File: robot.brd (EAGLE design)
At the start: 63.2 x 48.2 mm, 17 parts

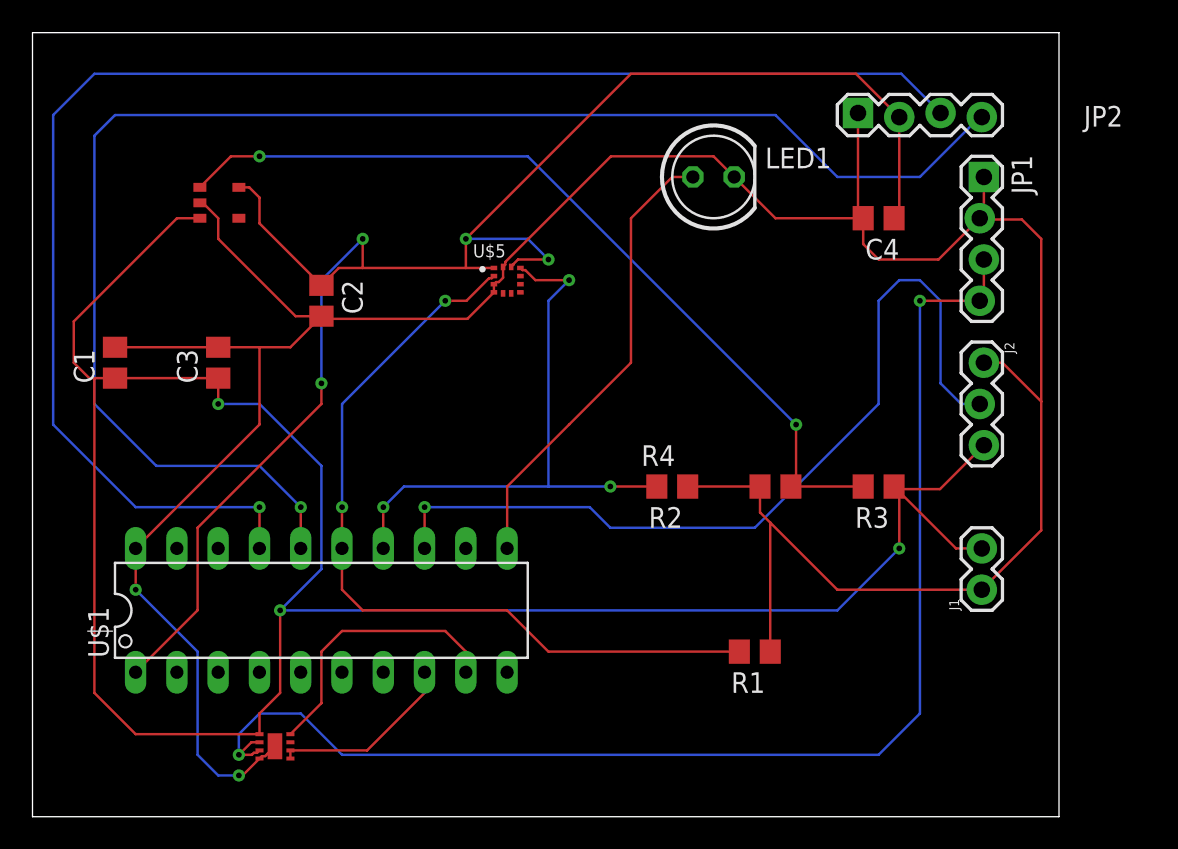
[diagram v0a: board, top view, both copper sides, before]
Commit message: Added power planes to board and also added a resistor for the LED.
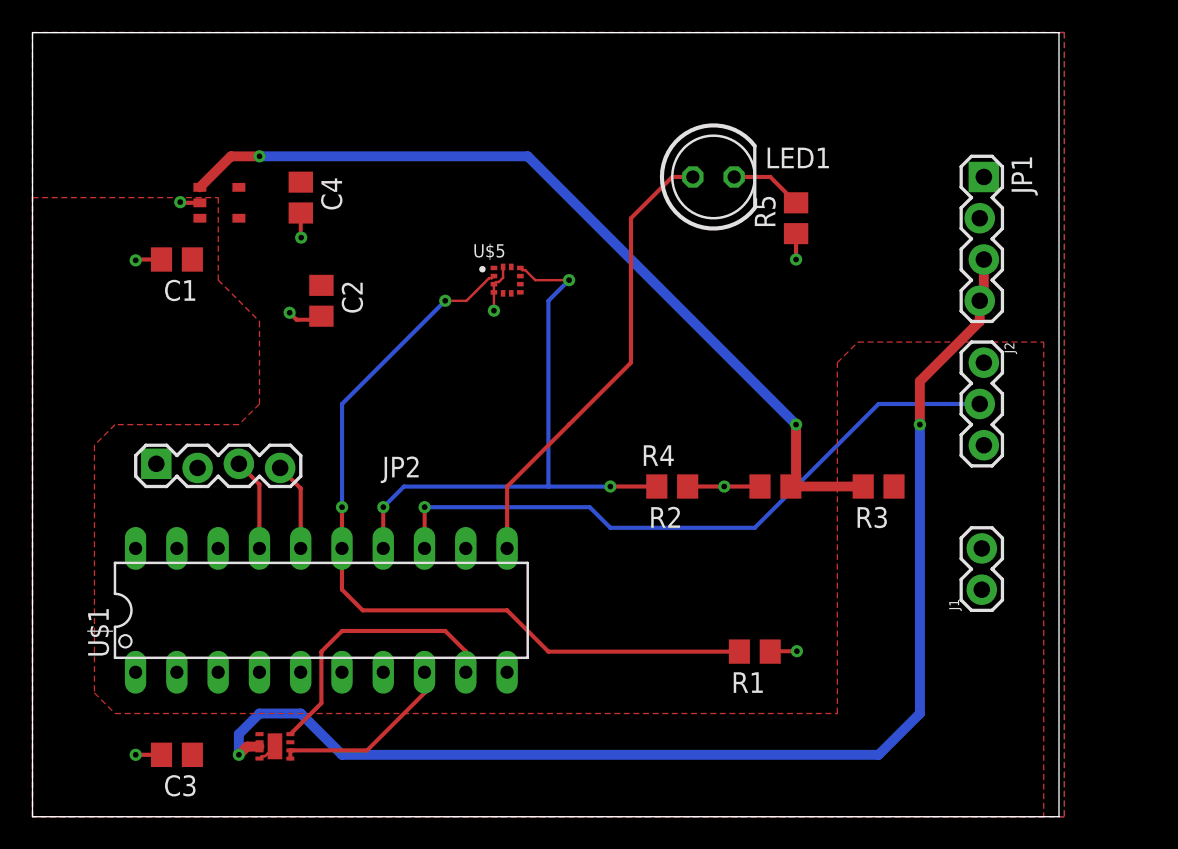
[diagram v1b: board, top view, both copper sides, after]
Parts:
- added R5: 330, rcl:R0805
- moved JP2 48.3 mm to (7.62, 48.3)
- moved C4 35.6 mm to (16.5, 64.8), turned to 270 degrees
- moved C3 24.3 mm to (8.89, 30.5), turned to 180 degrees
- moved C1 7.41 mm to (8.89, 61.0), turned to 180 degrees
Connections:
- net N$5 renamed 3V3_RAW
- net N$8 renamed MOTOR
- new net N$3: LED1.K, R5.2
- net 0: now also R5.1; no longer LED1.K
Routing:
- net 0: track 181.5 -> 20.7 mm, vias 2 -> 9
- net 4V5: track 137.5 -> 0.68 mm, vias 3 -> 0
- net 3V3: track 102.1 -> 0.00 mm, vias 4 -> 0
- net N$10: track 93.1 -> 5.73 mm, vias 1 -> 0
- net N$11: track 92.6 -> 5.48 mm, vias 1 -> 0
- net PWM_TA1.2: track 53.4 -> 40.4 mm
- net N$3: track 0.00 -> 4.47 mm
- net MOTOR: track 80.5 -> 77.4 mm
- added copper zone on layer 16, net 0
- added copper zone on layer 1, net 3V3
- added copper zone on layer 1, net 4V5
